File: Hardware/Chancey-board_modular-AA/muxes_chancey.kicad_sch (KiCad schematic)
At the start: 16 parts

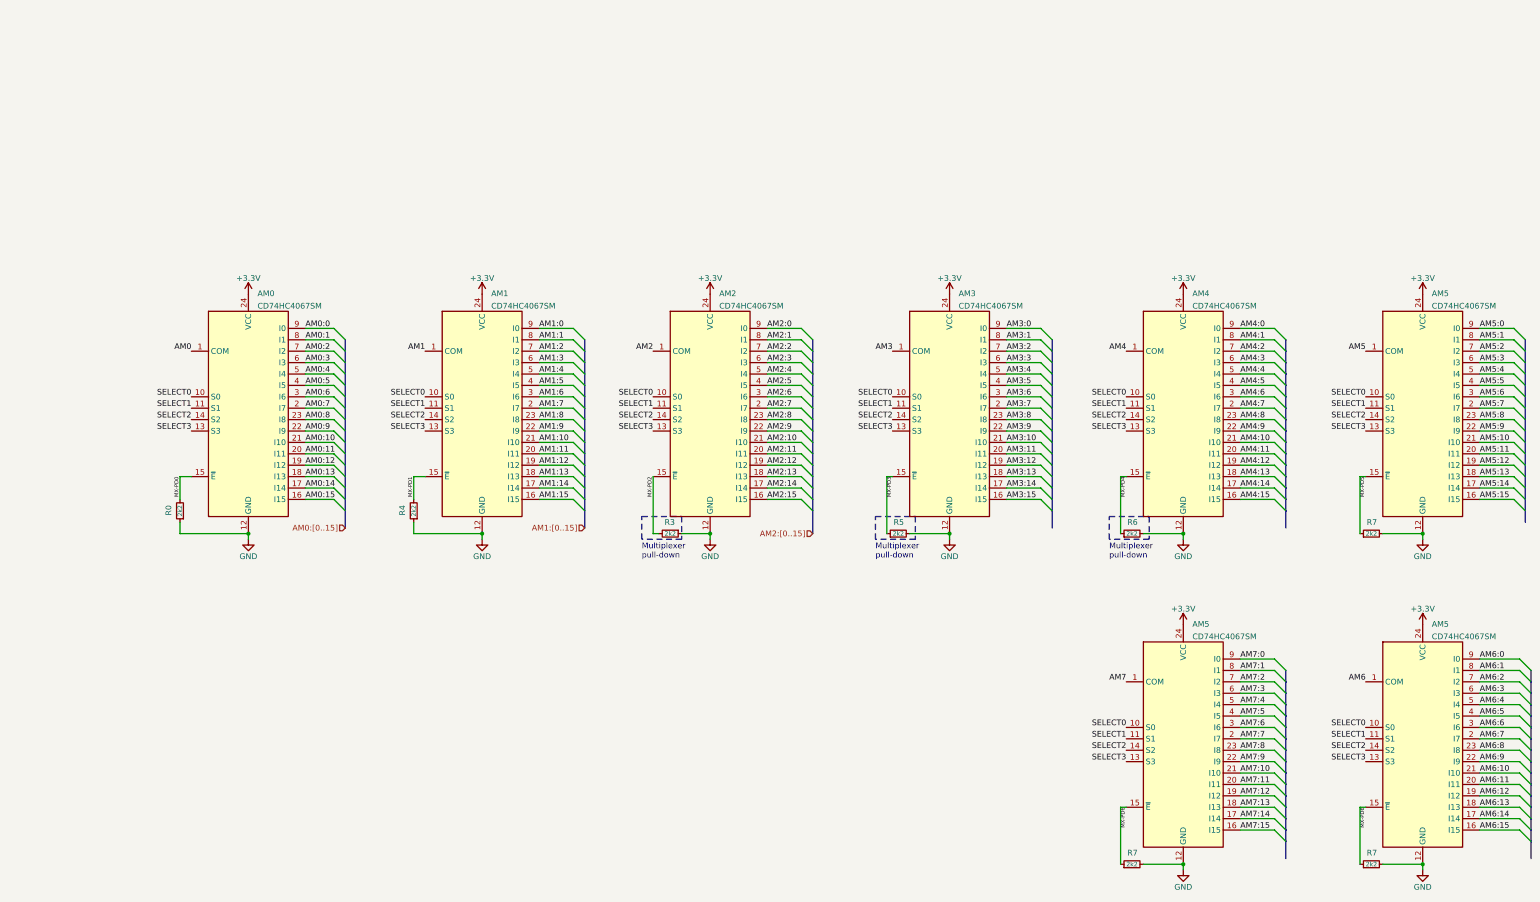
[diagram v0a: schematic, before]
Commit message: Changed many global labels to hierarchical and local labels.
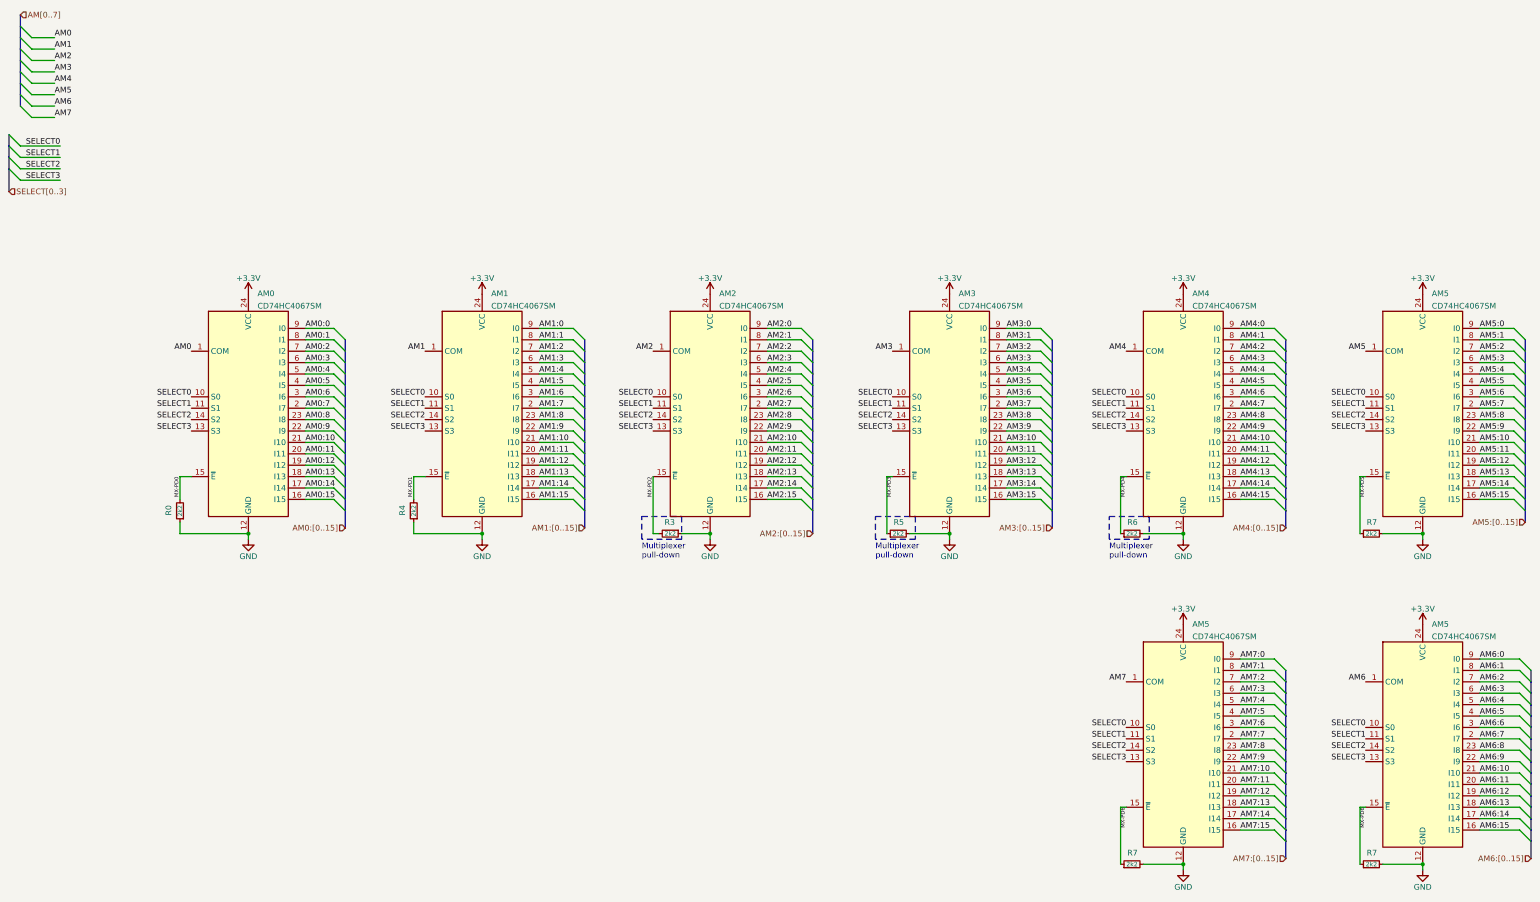
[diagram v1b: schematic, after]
